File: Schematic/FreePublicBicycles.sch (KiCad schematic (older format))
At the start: 36 parts

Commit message: Restructurized files
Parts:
- U?: symbol RF_Module:RFM95W-868S2 -> FreePublicBicycles-rescue:RFM95W-868S2-RF_Module
- U?: symbol Library:MP1584 -> FreePublicBicycles-rescue:MP1584-Library
- U?: symbol Library:S9V11F5 -> FreePublicBicycles-rescue:S9V11F5-Library
- U?: symbol Library:NEO-6M -> FreePublicBicycles-rescue:NEO-6M-Library
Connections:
- no-connect marks 4 -> 14
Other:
- moved on the sheet: C?, R?, SW?
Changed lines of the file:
@@
 EESchema Schematic File Version 4
 LIBS:FreePublicBicycles-cache
-EELAYER 29 0
+EELAYER 26 0
 EELAYER END
 $Descr A4 11693 8268
@@
 $EndComp
 $Comp
-L RF_Module:RFM95W-868S2 U?
+L FreePublicBicycles-rescue:RFM95W-868S2-RF_Module U?
 U 1 1 5E26F3C6
 P 8750 2950
@@
 $EndComp
 $Comp
-L Library:NEO-6M U?
+L FreePublicBicycles-rescue:NEO-6M-Library U?
 U 1 1 5E9303CF
-P 10200 4050
-F 0 "U?" H 10628 3863 50  0000 L CNN
-F 1 "NEO-6M" H 10628 3772 50  0000 L CNN
-F 2 "" H 10200 4050 50  0001 C CNN
-F 3 "" H 10200 4050 50  0001 C CNN
-	1    10200 4050
+P 9100 4300
+F 0 "U?" H 9528 4113 50  0000 L CNN
+F 1 "NEO-6M" H 9528 4022 50  0000 L CNN
+F 2 "" H 9100 4300 50  0001 C CNN
+F 3 "" H 9100 4300 50  0001 C CNN
+	1    9100 4300
 	0    1    1    0
 $EndComp
 Wire Wire Line
-	9750 4200 9600 4200
-Wire Wire Line
-	9750 4300 9600 4300
-Text GLabel 9600 4300 0    50   Input ~ 0
+	8650 4450 8500 4450
+Wire Wire Line
+	8650 4550 8500 4550
+Text GLabel 8500 4550 0    50   Input ~ 0
 RX
-Text GLabel 9600 4200 0    50   Input ~ 0
+Text GLabel 8500 4450 0    50   Input ~ 0
 TX
 Wire Wire Line
-	9750 4400 9600 4400
-Wire Wire Line
-	9750 4100 9600 4100
-Wire Wire Line
-	9600 4100 9600 4050
+	8650 4650 8500 4650
+Wire Wire Line
+	8650 4350 8500 4350
+Wire Wire Line
+	8500 4350 8500 4300
 $Comp
 L power:+5V #PWR?
 U 1 1 5E2D514F
-P 9600 4050
-F 0 "#PWR?" H 9600 3900 50  0001 C CNN
-F 1 "+5V" H 9615 4223 50  0000 C CNN
-F 2 "" H 9600 4050 50  0001 C CNN
-F 3 "" H 9600 4050 50  0001 C CNN
-	1    9600 4050
-	1    0    0    -1
-$EndComp
-Wire Wire Line
-	9600 4400 9600 4450
+P 8500 4300
+F 0 "#PWR?" H 8500 4150 50  0001 C CNN
+F 1 "+5V" H 8515 4473 50  0000 C CNN
+F 2 "" H 8500 4300 50  0001 C CNN
+F 3 "" H 8500 4300 50  0001 C CNN
+	1    8500 4300
+	1    0    0    -1
+$EndComp
+Wire Wire Line
+	8500 4650 8500 4700
 $Comp
 L power:GND #PWR?
 U 1 1 5E2D7839
-P 9600 4450
-F 0 "#PWR?" H 9600 4200 50  0001 C CNN
-F 1 "GND" H 9605 4277 50  0000 C CNN
-F 2 "" H 9600 4450 50  0001 C CNN
-F 3 "" H 9600 4450 50  0001 C CNN
-	1    9600 4450
-	1    0    0    -1
-$EndComp
-$Comp
-L Library:MP1584 U?
+P 8500 4700
+F 0 "#PWR?" H 8500 4450 50  0001 C CNN
+F 1 "GND" H 8505 4527 50  0000 C CNN
+F 2 "" H 8500 4700 50  0001 C CNN
+F 3 "" H 8500 4700 50  0001 C CNN
+	1    8500 4700
+	1    0    0    -1
+$EndComp
+$Comp
+L FreePublicBicycles-rescue:MP1584-Library U?
 U 1 1 5E634100
 P 5250 1250
@@
 $EndComp
 $Comp
-L Library:S9V11F5 U?
+L FreePublicBicycles-rescue:S9V11F5-Library U?
 U 1 1 5E63416C
 P 8050 1250
@@
 L Switch:SW_Push SW?
 U 1 1 5E660F0E
-P 9850 5500
-F 0 "SW?" H 9850 5785 50  0000 C CNN
-F 1 "Button" H 9850 5694 50  0000 C CNN
-F 2 "" H 9850 5700 50  0001 C CNN
-F 3 "~" H 9850 5700 50  0001 C CNN
-	1    9850 5500
-	1    0    0    -1
-$EndComp
-Wire Wire Line
-	10050 5500 10150 5500
-Wire Wire Line
-	10150 5500 10150 5800
+P 8750 5750
+F 0 "SW?" H 8750 6035 50  0000 C CNN
+F 1 "Button" H 8750 5944 50  0000 C CNN
+F 2 "" H 8750 5950 50  0001 C CNN
+F 3 "~" H 8750 5950 50  0001 C CNN
+	1    8750 5750
+	1    0    0    -1
+$EndComp
+Wire Wire Line
+	8950 5750 9050 5750
+Wire Wire Line
+	9050 5750 9050 6050
 $Comp
 L power:GND #PWR?
 U 1 1 5E671D81
-P 10150 5800
-F 0 "#PWR?" H 10150 5550 50  0001 C CNN
-F 1 "GND" H 10155 5627 50  0000 C CNN
-F 2 "" H 10150 5800 50  0001 C CNN
-F 3 "" H 10150 5800 50  0001 C CNN
-	1    10150 5800
-	1    0    0    -1
-$EndComp
-Text GLabel 8950 5500 0    50   Input ~ 0
+P 9050 6050
+F 0 "#PWR?" H 9050 5800 50  0001 C CNN
+F 1 "GND" H 9055 5877 50  0000 C CNN
+F 2 "" H 9050 6050 50  0001 C CNN
+F 3 "" H 9050 6050 50  0001 C CNN
+	1    9050 6050
+	1    0    0    -1
+$EndComp
+Text GLabel 7850 5750 0    50   Input ~ 0
 BUTTON
 Wire Wire Line
@@
 L Device:C_Small C?
 U 1 1 5E2EF3C9
-P 9550 5650
-F 0 "C?" H 9642 5696 50  0000 L CNN
-F 1 "100n" H 9642 5605 50  0000 L CNN
-F 2 "" H 9550 5650 50  0001 C CNN
-F 3 "~" H 9550 5650 50  0001 C CNN
-	1    9550 5650
-	1    0    0    -1
-$EndComp
-Wire Wire Line
-	9550 5750 9550 5800
-Wire Wire Line
-	9550 5500 9550 5550
-Wire Wire Line
-	9650 5500 9550 5500
+P 8450 5900
+F 0 "C?" H 8542 5946 50  0000 L CNN
+F 1 "100n" H 8542 5855 50  0000 L CNN
+F 2 "" H 8450 5900 50  0001 C CNN
+F 3 "~" H 8450 5900 50  0001 C CNN
+	1    8450 5900
+	1    0    0    -1
+$EndComp
+Wire Wire Line
+	8450 6000 8450 6050
+Wire Wire Line
+	8450 5750 8450 5800
+Wire Wire Line
+	8550 5750 8450 5750
 $Comp
 L Device:R R?
 U 1 1 5E3039C3
-P 9300 5500
-F 0 "R?" V 9450 5500 50  0000 L CNN
-F 1 "1k" V 9370 5455 50  0000 L CNN
-F 2 "" V 9230 5500 50  0001 C CNN
-F 3 "~" H 9300 5500 50  0001 C CNN
-	1    9300 5500
+P 8200 5750
+F 0 "R?" V 8350 5750 50  0000 L CNN
+F 1 "1k" V 8270 5705 50  0000 L CNN
+F 2 "" V 8130 5750 50  0001 C CNN
+F 3 "~" H 8200 5750 50  0001 C CNN
+	1    8200 5750
 	0    -1   -1   0
 $EndComp
 Wire Wire Line
-	9550 5500 9450 5500
-Connection ~ 9550 5500
-Wire Wire Line
-	8950 5500 9150 5500
+	8450 5750 8350 5750
+Connection ~ 8450 5750
+Wire Wire Line
+	7850 5750 8050 5750
 $Comp
 L power:GND #PWR?
 U 1 1 5E341971
-P 9550 5800
-F 0 "#PWR?" H 9550 5550 50  0001 C CNN
-F 1 "GND" H 9555 5627 50  0000 C CNN
-F 2 "" H 9550 5800 50  0001 C CNN
-F 3 "" H 9550 5800 50  0001 C CNN
-	1    9550 5800
+P 8450 6050
+F 0 "#PWR?" H 8450 5800 50  0001 C CNN
+F 1 "GND" H 8455 5877 50  0000 C CNN
+F 2 "" H 8450 6050 50  0001 C CNN
+F 3 "" H 8450 6050 50  0001 C CNN
+	1    8450 6050
 	1    0    0    -1
 $EndComp
@@
 Text GLabel 3350 3950 2    50   Input ~ 0
 TX
+NoConn ~ 3150 4850
+NoConn ~ 3150 4950
+NoConn ~ 3150 5050
+NoConn ~ 3150 5150
+NoConn ~ 3150 5250
+NoConn ~ 3150 5550
+NoConn ~ 3150 5650
+NoConn ~ 3150 5950
+NoConn ~ 3150 6150
+NoConn ~ 3150 6250
 $EndSCHEMATC

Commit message: Added GPS control logic
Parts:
- added Q1: PN2222A, Package_TO_SOT_THT:TO-92_Inline, symbol Transistor_BJT:PN2222A
- added Q2: IRF4905, Package_TO_SOT_THT:TO-220-3_Vertical, symbol Transistor_FET:IRF4905
- added R3: 1k, symbol Device:R
- added R4: 4.7k, symbol Device:R
- gave numbers to parts that had none: 36
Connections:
- net +5V: now also Q2.3 (S), R4.2; no longer U6.1 (VCC)
- net GND: now also Q1.1 (E)
- net GPSEN: now reaches U1.28 (PC5)
- net GPSEN: now also R3.2
- new net: Q1.2 (B), R3.1
- new net: Q1.3 (C), Q2.1 (G), R4.1
- new net VCCGPS: Q2.2 (D), U6.1 (VCC)
- no-connect marks 14 -> 13
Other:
- moved on the sheet: C15, R2, SW1, U6

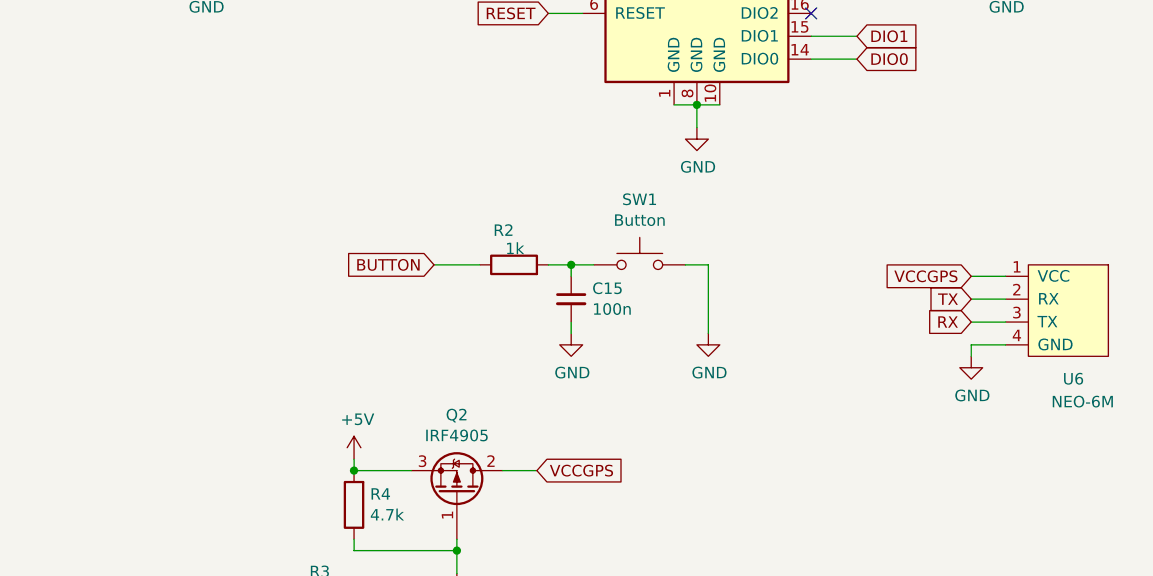
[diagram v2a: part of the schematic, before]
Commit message: fixed PCB layout and transmitter data fetch bug
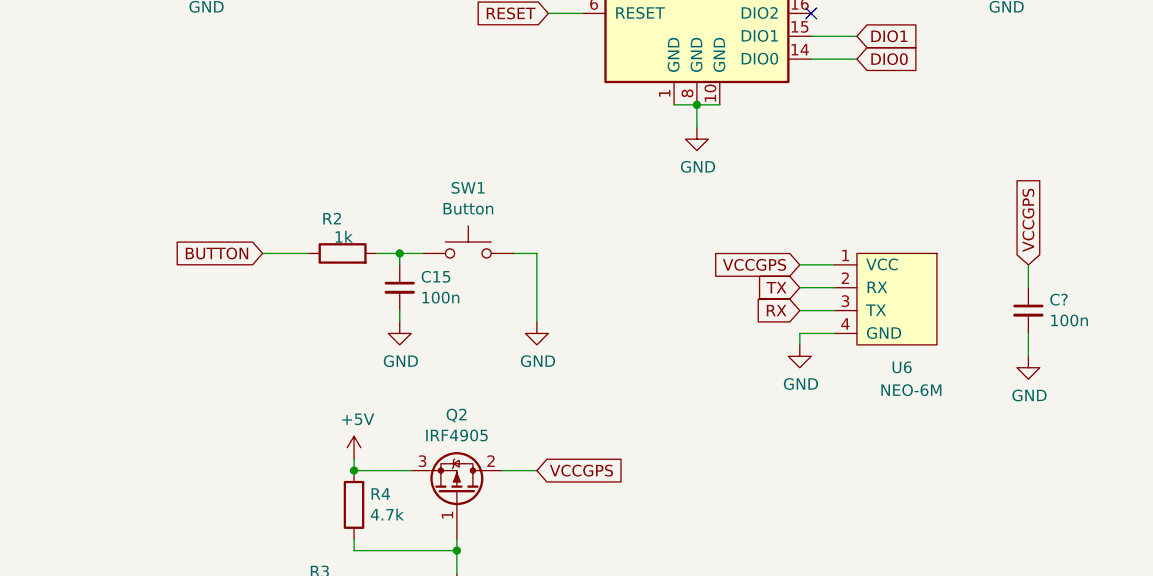
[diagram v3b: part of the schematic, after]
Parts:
- added C?: 100n, symbol Device:C_Small
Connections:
- net GND: now also C?.2
- net VCCGPS: now also C?.1
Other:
- moved on the sheet: C15, R2, SW1, U6
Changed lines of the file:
@@
 L FreePublicBicycles-rescue:NEO-6M-Library U6
 U 1 1 5E9303CF
-P 10550 4250
-F 0 "U6" V 11050 4050 50  0000 L CNN
-F 1 "NEO-6M" V 11150 4000 50  0000 L CNN
-F 2 "" H 10550 4250 50  0001 C CNN
-F 3 "" H 10550 4250 50  0001 C CNN
-	1    10550 4250
+P 9800 4200
+F 0 "U6" V 10300 4000 50  0000 L CNN
+F 1 "NEO-6M" V 10400 3950 50  0000 L CNN
+F 2 "" H 9800 4200 50  0001 C CNN
+F 3 "" H 9800 4200 50  0001 C CNN
+	1    9800 4200
 	0    1    1    0
 $EndComp
 Wire Wire Line
-	10100 4400 9950 4400
-Wire Wire Line
-	10100 4500 9950 4500
-Text GLabel 9950 4500 0    50   Input ~ 0
+	9350 4350 9200 4350
+Wire Wire Line
+	9350 4450 9200 4450
+Text GLabel 9200 4450 0    50   Input ~ 0
 RX
-Text GLabel 9950 4400 0    50   Input ~ 0
+Text GLabel 9200 4350 0    50   Input ~ 0
 TX
 Wire Wire Line
-	10100 4600 9950 4600
-Wire Wire Line
-	10100 4300 9950 4300
-Wire Wire Line
-	9950 4600 9950 4650
+	9350 4550 9200 4550
+Wire Wire Line
+	9350 4250 9200 4250
+Wire Wire Line
+	9200 4550 9200 4600
 $Comp
 L power:GND #PWR020
 U 1 1 5E2D7839
-P 9950 4650
-F 0 "#PWR020" H 9950 4400 50  0001 C CNN
-F 1 "GND" H 9955 4477 50  0000 C CNN
-F 2 "" H 9950 4650 50  0001 C CNN
-F 3 "" H 9950 4650 50  0001 C CNN
-	1    9950 4650
+P 9200 4600
+F 0 "#PWR020" H 9200 4350 50  0001 C CNN
+F 1 "GND" H 9205 4427 50  0000 C CNN
+F 2 "" H 9200 4600 50  0001 C CNN
+F 3 "" H 9200 4600 50  0001 C CNN
+	1    9200 4600
 	1    0    0    -1
 $EndComp
@@
 L Switch:SW_Push SW1
 U 1 1 5E660F0E
-P 8500 4250
-F 0 "SW1" H 8500 4535 50  0000 C CNN
-F 1 "Button" H 8500 4444 50  0000 C CNN
-F 2 "" H 8500 4450 50  0001 C CNN
-F 3 "~" H 8500 4450 50  0001 C CNN
-	1    8500 4250
-	1    0    0    -1
-$EndComp
-Wire Wire Line
-	8700 4250 8800 4250
-Wire Wire Line
-	8800 4250 8800 4550
+P 7750 4200
+F 0 "SW1" H 7750 4485 50  0000 C CNN
+F 1 "Button" H 7750 4394 50  0000 C CNN
+F 2 "" H 7750 4400 50  0001 C CNN
+F 3 "~" H 7750 4400 50  0001 C CNN
+	1    7750 4200
+	1    0    0    -1
+$EndComp
+Wire Wire Line
+	7950 4200 8050 4200
+Wire Wire Line
+	8050 4200 8050 4500
 $Comp
 L power:GND #PWR017
 U 1 1 5E671D81
-P 8800 4550
-F 0 "#PWR017" H 8800 4300 50  0001 C CNN
-F 1 "GND" H 8805 4377 50  0000 C CNN
-F 2 "" H 8800 4550 50  0001 C CNN
-F 3 "" H 8800 4550 50  0001 C CNN
-	1    8800 4550
-	1    0    0    -1
-$EndComp
-Text GLabel 7600 4250 0    50   Input ~ 0
+P 8050 4500
+F 0 "#PWR017" H 8050 4250 50  0001 C CNN
+F 1 "GND" H 8055 4327 50  0000 C CNN
+F 2 "" H 8050 4500 50  0001 C CNN
+F 3 "" H 8050 4500 50  0001 C CNN
+	1    8050 4500
+	1    0    0    -1
+$EndComp
+Text GLabel 6850 4200 0    50   Input ~ 0
 BUTTON
 Wire Wire Line
@@
 L Device:C_Small C15
 U 1 1 5E2EF3C9
-P 8200 4400
-F 0 "C15" H 8292 4446 50  0000 L CNN
-F 1 "100n" H 8292 4355 50  0000 L CNN
-F 2 "" H 8200 4400 50  0001 C CNN
-F 3 "~" H 8200 4400 50  0001 C CNN
-	1    8200 4400
-	1    0    0    -1
-$EndComp
-Wire Wire Line
-	8200 4500 8200 4550
-Wire Wire Line
-	8200 4250 8200 4300
-Wire Wire Line
-	8300 4250 8200 4250
+P 7450 4350
+F 0 "C15" H 7542 4396 50  0000 L CNN
+F 1 "100n" H 7542 4305 50  0000 L CNN
+F 2 "" H 7450 4350 50  0001 C CNN
+F 3 "~" H 7450 4350 50  0001 C CNN
+	1    7450 4350
+	1    0    0    -1
+$EndComp
+Wire Wire Line
+	7450 4450 7450 4500
+Wire Wire Line
+	7450 4200 7450 4250
+Wire Wire Line
+	7550 4200 7450 4200
 $Comp
 L Device:R R2
 U 1 1 5E3039C3
-P 7950 4250
-F 0 "R2" V 8100 4250 50  0000 L CNN
-F 1 "1k" V 8020 4205 50  0000 L CNN
-F 2 "" V 7880 4250 50  0001 C CNN
-F 3 "~" H 7950 4250 50  0001 C CNN
-	1    7950 4250
+P 7200 4200
+F 0 "R2" V 7350 4200 50  0000 L CNN
+F 1 "1k" V 7270 4155 50  0000 L CNN
+F 2 "" V 7130 4200 50  0001 C CNN
+F 3 "~" H 7200 4200 50  0001 C CNN
+	1    7200 4200
 	0    -1   -1   0
 $EndComp
 Wire Wire Line
-	8200 4250 8100 4250
-Connection ~ 8200 4250
-Wire Wire Line
-	7600 4250 7800 4250
+	7450 4200 7350 4200
+Connection ~ 7450 4200
+Wire Wire Line
+	6850 4200 7050 4200
 $Comp
 L power:GND #PWR014
 U 1 1 5E341971
-P 8200 4550
-F 0 "#PWR014" H 8200 4300 50  0001 C CNN
-F 1 "GND" H 8205 4377 50  0000 C CNN
-F 2 "" H 8200 4550 50  0001 C CNN
-F 3 "" H 8200 4550 50  0001 C CNN
-	1    8200 4550
+P 7450 4500
+F 0 "#PWR014" H 7450 4250 50  0001 C CNN
+F 1 "GND" H 7455 4327 50  0000 C CNN
+F 2 "" H 7450 4500 50  0001 C CNN
+F 3 "" H 7450 4500 50  0001 C CNN
+	1    7450 4500
 	1    0    0    -1
 $EndComp
@@
 Text GLabel 3350 5250 2    50   Input ~ 0
 GPSEN
-Text GLabel 9950 4300 0    50   Input ~ 0
+Text GLabel 9200 4250 0    50   Input ~ 0
 VCCGPS
 Text GLabel 6800 5800 0    50   Input ~ 0
@@
 Text GLabel 8050 5150 2    50   Input ~ 0
 VCCGPS
+Wire Wire Line
+	10200 4350 10200 4250
+Text GLabel 10200 4250 1    50   Input ~ 0
+VCCGPS
+$Comp
+L Device:C_Small C?
+U 1 1 5E33270D
+P 10200 4450
+F 0 "C?" H 10292 4496 50  0000 L CNN
+F 1 "100n" H 10292 4405 50  0000 L CNN
+F 2 "" H 10200 4450 50  0001 C CNN
+F 3 "~" H 10200 4450 50  0001 C CNN
+	1    10200 4450
+	1    0    0    -1
+$EndComp
+$Comp
+L power:GND #PWR?
+U 1 1 5E33A56C
+P 10200 4650
+F 0 "#PWR?" H 10200 4400 50  0001 C CNN
+F 1 "GND" H 10205 4477 50  0000 C CNN
+F 2 "" H 10200 4650 50  0001 C CNN
+F 3 "" H 10200 4650 50  0001 C CNN
+	1    10200 4650
+	1    0    0    -1
+$EndComp
+Wire Wire Line
+	10200 4550 10200 4650
 $EndSCHEMATC

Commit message: Updated Schematic and PCB
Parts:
- removed J1: Dynamo, symbol Connector:Screw_Terminal_01x02
- added J1: Conn_01x04_Female, symbol Connector:Conn_01x04_Female
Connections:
- net BUTTON: now also U1.5 (PD3); no longer U1.23 (PC0)
- net at D2.1 (K), D4.2 (A): now also J1.3 (Pin_3), J1.4 (Pin_4)
- net at D1.1 (K), D3.2 (A): now also J1.1 (Pin_1), J1.2 (Pin_2)
- net DIO1: no longer names the net of U5.15 (DIO1)
- net DIO1: no longer U1.5 (PD3)
- no-connect marks 13 -> 15
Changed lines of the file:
@@
 	9250 3350 9450 3350
-Wire Wire Line
-	9250 3250 9450 3250
 Wire Wire Line
 	8850 3550 8750 3550
@@
 Text GLabel 3350 5750 2    50   Input ~ 0
 DIO0
-Wire Wire Line
-	3150 5850 3350 5850
-Text GLabel 9450 3250 2    50   Input ~ 0
-DIO1
-Text GLabel 3350 5850 2    50   Input ~ 0
-DIO1
 NoConn ~ 9250 3150
 NoConn ~ 9250 3050
@@
 	2400 1050 2300 1050
 $Comp
-L Connector:Screw_Terminal_01x02 J1
-U 1 1 5E63414E
-P 1850 1300
-F 0 "J1" H 1850 950 50  0000 C CNN
-F 1 "Dynamo" H 1850 1050 50  0000 C CNN
-F 2 "" H 1850 1300 50  0001 C CNN
-F 3 "~" H 1850 1300 50  0001 C CNN
-	1    1850 1300
-	-1   0    0    1
-$EndComp
-$Comp
 L Device:D_Schottky_ALT D1
 U 1 1 5E634154
@@
 	6450 1650 6850 1650
 Wire Wire Line
-	3150 4750 3350 4750
-Text GLabel 3350 4750 2    50   Input ~ 0
+	3150 5850 3350 5850
+Text GLabel 3350 5850 2    50   Input ~ 0
 BUTTON
 $Comp
@@
 Wire Wire Line
 	10200 4550 10200 4650
+Wire Wire Line
+	2050 1300 1950 1300
+Wire Wire Line
+	1950 1200 2050 1200
+$Comp
+L Connector:Conn_01x04_Female J1
+U 1 1 5E3432F6
+P 1750 1200
+F 0 "J1" H 1644 1485 50  0000 C CNN
+F 1 "Conn_01x04_Female" H 1644 1394 50  0000 C CNN
+F 2 "" H 1750 1200 50  0001 C CNN
+F 3 "~" H 1750 1200 50  0001 C CNN
+	1    1750 1200
+	-1   0    0    -1
+$EndComp
+Wire Wire Line
+	1950 1200 1950 1100
+Connection ~ 1950 1200
+Wire Wire Line
+	1950 1300 1950 1400
+Connection ~ 1950 1300
+NoConn ~ 3150 4750
+NoConn ~ 9250 3250
 $EndSCHEMATC
